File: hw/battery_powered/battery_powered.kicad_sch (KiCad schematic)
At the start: 64 parts, among them J101 5077CR-16SMC2-BK-TR, J102 battery_wire_pad, J103 BM03B-SRSS-TB(LF)(SN)_pico_de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, J104 10029449-111RLF, SW101 SS12D01G4, SW102 SKRPABE010, SW103 SKRPABE010, SW104 SKRPABE010, U101 RT6150B-33GQW, U102 W25Q16JVSNIQ, U103 RP2040, U104 PCA9306D, U105 OSL10564-IB, U106 chofutech_logo, Y101 FA-238V

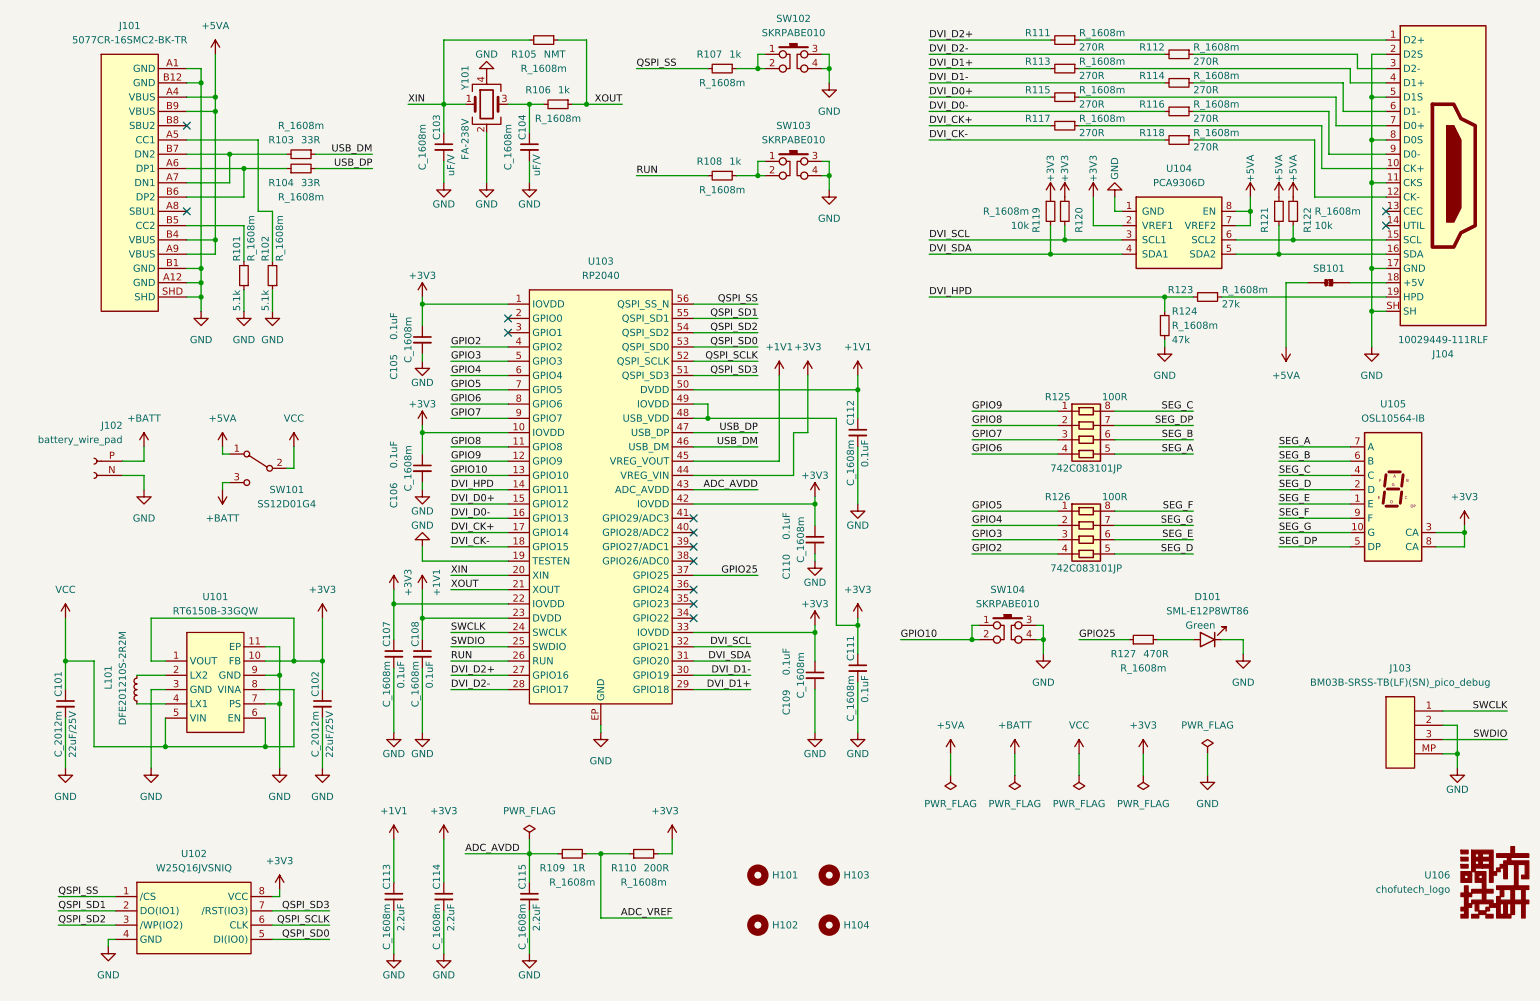
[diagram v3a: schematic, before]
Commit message: change DVI pin assignment (PicoDVI cfg written in schematic)
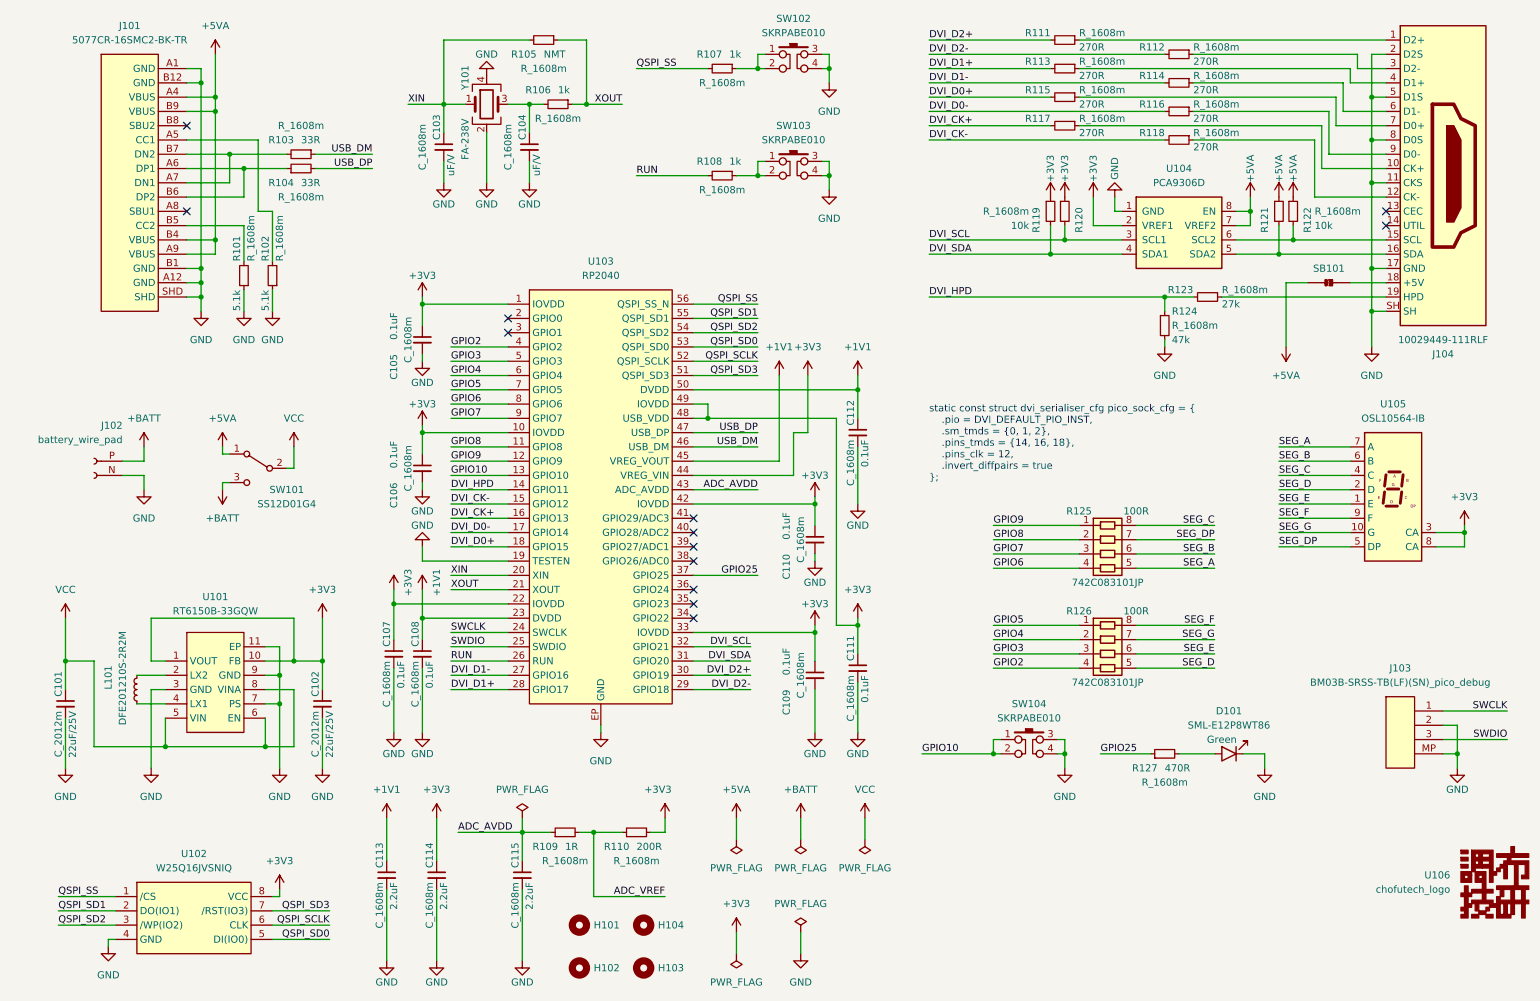
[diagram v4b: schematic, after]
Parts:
- H101, H102, H103, H104: footprint 00_custom_lib:MountingHole_2.2mm_M2 -> 00_custom_lib:MountingHole_3.2mm_M3
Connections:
- net DVI_CK+: now also U103.16 (GPIO13); no longer U103.17 (GPIO14)
- net DVI_CK-: now also U103.15 (GPIO12); no longer U103.18 (GPIO15)
- net DVI_D0+: now also U103.18 (GPIO15); no longer U103.15 (GPIO12)
- net DVI_D0-: now also U103.17 (GPIO14); no longer U103.16 (GPIO13)
- net DVI_D1+: now also U103.28 (GPIO17); no longer U103.29 (GPIO18)
- net DVI_D1-: now also U103.27 (GPIO16); no longer U103.30 (GPIO19)
- net DVI_D2+: now also U103.30 (GPIO19); no longer U103.27 (GPIO16)
- net DVI_D2-: now also U103.29 (GPIO18); no longer U103.28 (GPIO17)
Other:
- note added: "static const struct dvi_serialiser_cfg pico_sock_cfg = { .pio = DVI_DEFAULT_PIO_INST, .sm_tmds = {0, 1, 2}, .pins_tmds = {14, 16, 18}, .pins_clk = 12, .invert_diffpairs = true };"
- moved on the sheet: C113, C114, C115, D101, H101, H102, H103, H104, R109, R110, R125, R126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
